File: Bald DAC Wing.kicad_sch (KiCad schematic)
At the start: 29 parts, among them U1 OPA365AIDBVTG4

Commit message: First pass schematic. going to give to clanker to see if it can populate the pcb logically.
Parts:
- added C1, C2, C3, C4: C, Capacitor_SMD:C_0805_2012Metric_Pad1.18x1.45mm_HandSolder, symbol Device:C
- added D1, D2, D3, D4: Power, symbol Device:LED
- added H1, H2, H3, H4: MountingHole_M2.5_Screw, MountingHole:MountingHole_2.7mm_M2.5, symbol My Library:MountingHole_M2.5_Screw
- added J1: Power, symbol Connector_Generic:Conn_01x04
- added J2: DAC_A_Out, symbol Connector_Generic:Conn_01x03
- added J3: DAC_B_Out, symbol Connector_Generic:Conn_01x03
- added R0, R31, R33, R35, R37, R39, R41, R43, R45, R47, R49, R51, R53, R55, R57: 20k, Capacitor_SMD:C_0402_1005Metric_Pad0.74x0.62mm_HandSolder, symbol Device:R
- added R29, R30, R58, R59: 0, Resistor_SMD:R_1206_3216Metric_Pad1.30x1.75mm_HandSolder, symbol Device:R
- added R32, R34, R36, R38, R40, R42, R44, R46, R48, R50, R52, R54, R56: 10k, Capacitor_SMD:C_0402_1005Metric_Pad0.74x0.62mm_HandSolder, symbol Device:R
- added R61, R62, R63, R64: 1k, Resistor_SMD:R_0603_1608Metric_Pad0.98x0.95mm_HandSolder, symbol Device:R
- added TP1, TP2, TP3, TP4, TP5, TP6: TestPoint, My Libraries:Harwin-S1751-46-Test-Point, symbol My Library:TestPoint_Harwin
- added U2: OPA365AIDBVTG4, Package_TO_SOT_SMD:SOT-23-5, symbol Amplifier_Operational:OPA365xxDBV
- R1, R10, R11, R12, R13, R14, R15, R16, R17, R18, R19, R2, R20, R21, R22, R23, R24, R25, R26, R27, R28, R3, R4, R5, R6, R7, R8, R9: footprint (none) -> Capacitor_SMD:C_0402_1005Metric_Pad0.74x0.62mm_HandSolder
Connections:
- net GND: now also C1.2, C2.2, C3.2, C4.2, J1.3 (Pin_3), J1.4 (Pin_4), J2.2 (Pin_2), J2.3 (Pin_3), J3.2 (Pin_2), J3.3 (Pin_3), R31.2, R61.1, R62.1, R63.1, R64.1; no longer U1.2 (V-)
- net VCC: now also C1.1, C2.1, D1.2 (A), D2.2 (A), J1.1 (Pin_1), U2.5 (V+)
- net at R26.2, R27.1: now also R12.2; no longer R13.2
- net at R19.2, R20.1: now also R5.2; no longer R6.2
- net at R20.2, R21.1: now also R6.2; no longer R7.2
- net at R15.1, R28.1: now also R0.2; no longer R1.2
- net at U1.1: now also R29.1; no longer U1.4 (-)
- net at R15.2, R16.1: now also R1.2; no longer R2.2
- net at R21.2, R22.1: now also R7.2; no longer R8.2
- net at R23.2, R24.1: now also R9.2; no longer R10.2
- net at R25.2, R26.1: now also R11.2; no longer R12.2
- net at R22.2, R23.1: now also R8.2; no longer R9.2
- net at R18.2, R19.1: now also R4.2; no longer R5.2
- net at R17.2, R18.1: now also R3.2; no longer R4.2
- net at R24.2, R25.1: now also R10.2; no longer R11.2
- net at R16.2, R17.1: now also R2.2; no longer R3.2
- net D0_LSB renamed A1
- net D1 renamed A2
- net D10 renamed A11
- net D11 renamed A12
- net D12 renamed A13
- net D13_MSB renamed B0
- net D2 renamed A3
- net D3 renamed A4
- net D4 renamed A5
- net D5 renamed A6
- net D6 renamed A7
- net D7 renamed A8
- net D8 renamed A9
- net D9 renamed A10
- removed net VOUT_DAC: R14.2, R27.2, U1.3 (+)
- new net: R40.2, R41.2, R42.1
- new net: R42.2, R43.2, R44.1
- new net: R34.2, R35.2, R36.1
- new net: D4.2 (A), R64.2
- new net: R30.2, TP2.1, U1.3 (+)
- new net: R52.2, R53.2, R54.1
- new net: R44.2, R45.2, R46.1
- new net: R14.2, R31.1, R32.1
- new net: R32.2, R33.2, R34.1
- new net: R50.2, R51.2, R52.1
- new net: R36.2, R37.2, R38.1
- new net: R46.2, R47.2, R48.1
- new net: R58.2, TP5.1, U2.3 (+)
- new net: R54.2, R55.2, R56.1
- new net: R38.2, R39.2, R40.1
- new net: D3.2 (A), R63.2
- new net: R48.2, R49.2, R50.1
- new net: R59.1, U2.1
- new net: D2.1 (K), R62.2
- new net: D1.1 (K), R61.2
- new net A0: R0.1
- new net B1: R33.1
- new net B10: R51.1
- new net B11: R53.1
- new net B12: R55.1
- new net B13: R57.1
- new net B2: R35.1
- new net B3: R37.1
- new net B4: R39.1
- new net B5: R41.1
- new net B6: R43.1
- new net B7: R45.1
- new net B8: R47.1
- new net B9: R49.1
- new net OUT_A: J2.1 (Pin_1), R29.2, TP1.1, U1.4 (-)
- new net OUT_B: J3.1 (Pin_1), R59.2, TP6.1, U2.4 (-)
- new net VEE: C3.1, C4.1, D3.1 (K), D4.1 (K), J1.2 (Pin_2), U1.2 (V-), U2.2 (V-)
- new net VOUT_DAC_A: R13.2, R27.2, R30.1, TP3.1
- new net VOUT_DAC_B: R56.2, R57.2, R58.1, TP4.1
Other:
- note added: "-5"
- note added: "0"
- note added: "Need Blue or White LED to use with 10k. Check price of Green + R cost."
- note added: "Todo: BE Logo Symbol"
- moved on the sheet: R15, R16, R17, R18, R19, R20, R21, R22, R23, R24, R25, R26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

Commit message: bailing on discrete version. makes no sense.
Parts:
- added A1: RaspberryPi_Pico, Module:RaspberryPi_Pico_Common_Unspecified, symbol MCU_Module:RaspberryPi_Pico
- C1, C2, C3, C4: value C -> 1u; LCSC (none) -> C28323
- D1: value Power -> PwrA+; footprint (none) -> LED_SMD:LED_0805_2012Metric_Pad1.15x1.40mm_HandSolder; LCSC (none) -> C7496832
- D2: value Power -> PwrB+; footprint (none) -> LED_SMD:LED_0805_2012Metric_Pad1.15x1.40mm_HandSolder; LCSC (none) -> C7496832
- D3: value Power -> PwrA-; footprint (none) -> LED_SMD:LED_0805_2012Metric_Pad1.15x1.40mm_HandSolder; LCSC (none) -> C7496832
- D4: value Power -> PwrB-; footprint (none) -> LED_SMD:LED_0805_2012Metric_Pad1.15x1.40mm_HandSolder; LCSC (none) -> C7496832
- H1, H2, H3, H4: LCSC (none) -> N/A
- J1: value Power -> Power_In; footprint (none) -> LED_SMD:LED_0805_2012Metric_Pad1.15x1.40mm_HandSolder; LCSC (none) -> N/A
- J2, J3: footprint (none) -> Connector_PinHeader_2.54mm:PinHeader_1x03_P2.54mm_Vertical; LCSC (none) -> N/A
- R61, R62, R63, R64: LCSC C5184071 -> (none)
- TP1, TP2, TP3, TP4, TP5, TP6: LCSC (none) -> C3029083
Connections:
- new net: A1.13 (GND), A1.18 (GND), A1.23 (GND), A1.28 (GND), A1.3 (GND), A1.38 (GND), A1.8 (GND)
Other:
- note added: "1. Need Reset and Boot(how?) buttons on shield. 2. Need 1 signal for blanking. 3. Add Tek probe adapters?"
- note removed: "Need Blue or White LED to use with 10k. Check price of Green + R cost."
- moved on the sheet: H1, H2, H3, H4

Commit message: starting over with ICs
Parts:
- removed R0, R1, R10, R11, R12, R13, R14, R2, R28, R3, R31, R33, R35, R37, R39, R4, R41, R43, R45, R47, R49, R5, R51, R53, R55, R57, R6, R7, R8, R9: 20k, Capacitor_SMD:C_0402_1005Metric_Pad0.74x0.62mm_HandSolder, symbol Device:R
- removed R15, R16, R17, R18, R19, R20, R21, R22, R23, R24, R25, R26, R27, R32, R34, R36, R38, R40, R42, R44, R46, R48, R50, R52, R54, R56: 10k, Capacitor_SMD:C_0402_1005Metric_Pad0.74x0.62mm_HandSolder, symbol Device:R
- removed R29, R30, R58, R59: 0, Resistor_SMD:R_1206_3216Metric_Pad1.30x1.75mm_HandSolder, symbol Device:R
- removed TP1, TP2, TP3, TP4, TP5, TP6: TestPoint, My Libraries:Harwin-S1751-46-Test-Point, symbol My Library:TestPoint_Harwin
- removed U1, U2: OPA365AIDBVTG4, Package_TO_SOT_SMD:SOT-23-5, symbol Amplifier_Operational:OPA365xxDBV
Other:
- note added: "1. Need Reset and Boot(how?) buttons on shield. 2. Need 1 signal for blanking. 3. Add Tek probe adapters? Looking at AD5447 (C514217) 12-bit DAC. Check its datasheet what op-amp buffers it is using."
- note removed: "1. Need Reset and Boot(how?) buttons on shield. 2. Need 1 signal for blanking. 3. Add Tek probe adapters?"

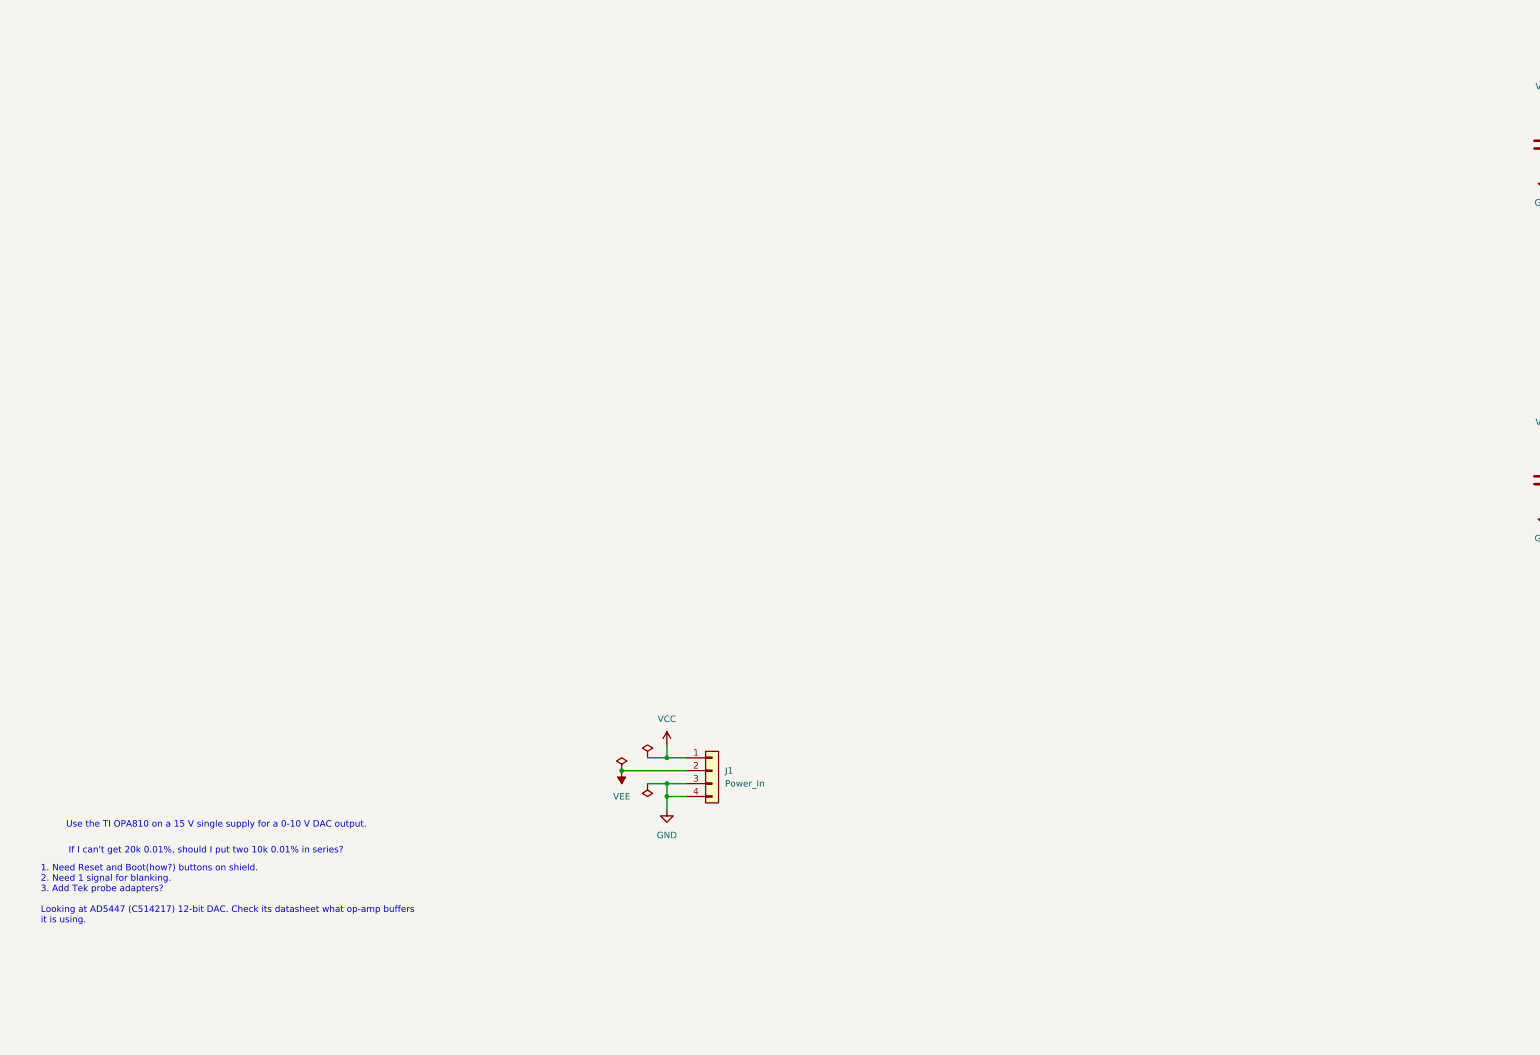
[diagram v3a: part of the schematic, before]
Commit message: latches in place. need to decide on VEE and what to use for Vref (ADR03?)
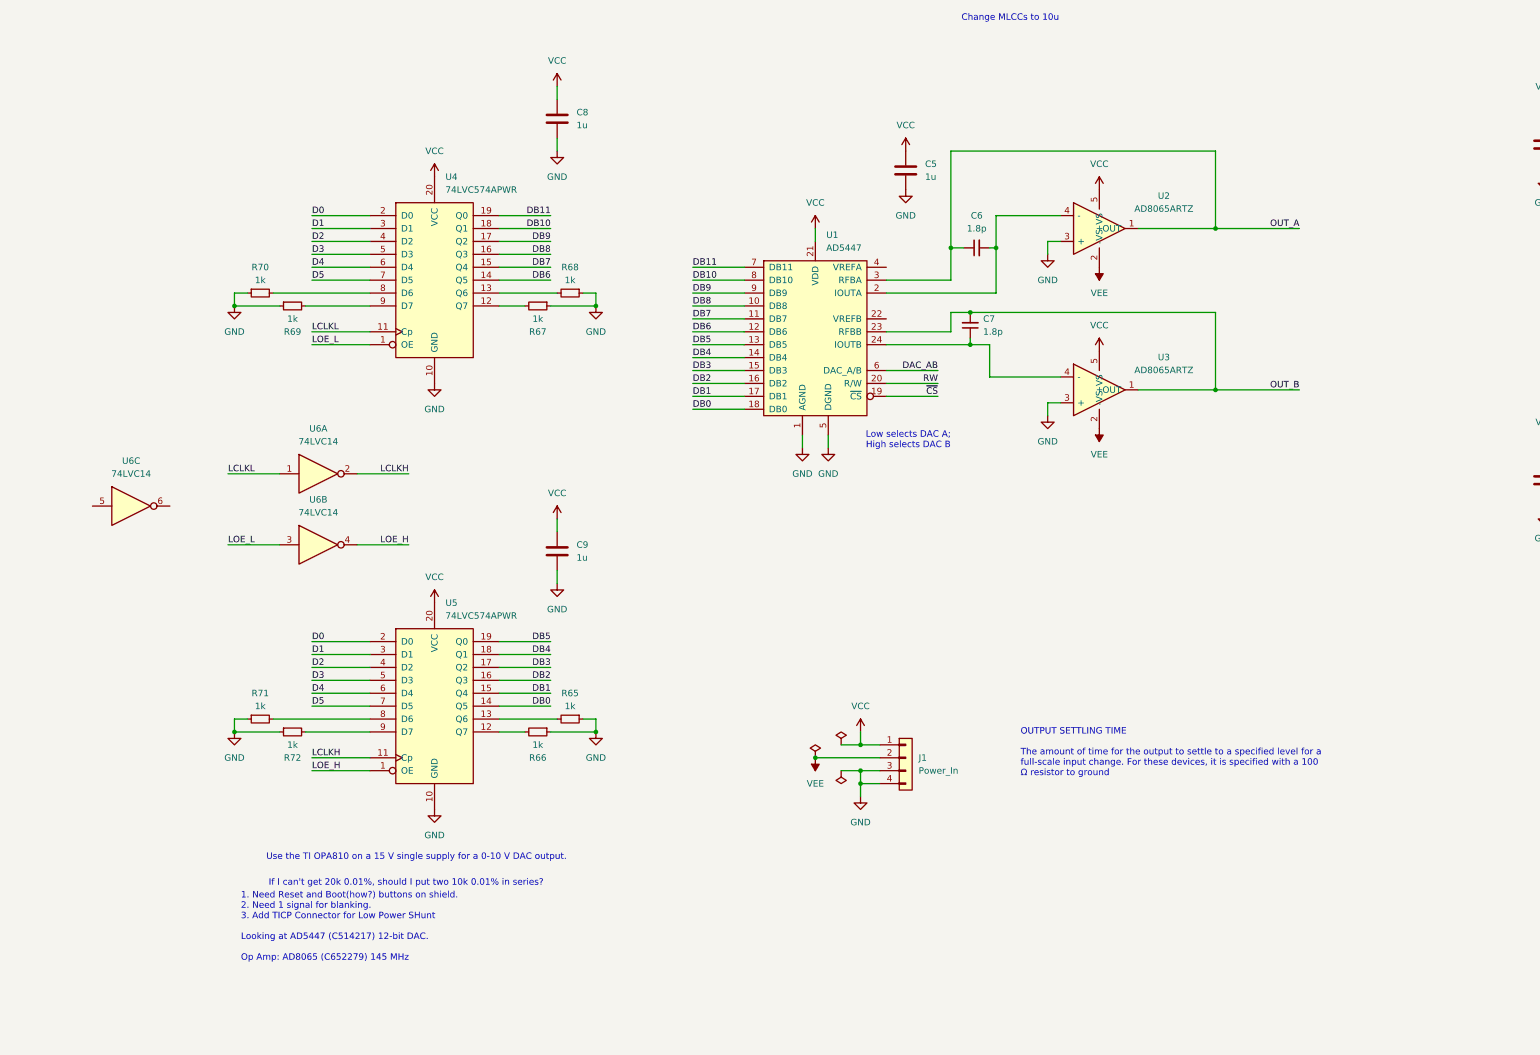
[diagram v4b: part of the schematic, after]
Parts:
- added C5, C8, C9: 1u, Capacitor_SMD:C_0805_2012Metric_Pad1.18x1.45mm_HandSolder, symbol Device:C
- added C6, C7: 1.8p, symbol Device:C_Small
- added R65, R66, R67, R68, R69, R70, R71, R72: 1k, Resistor_SMD:R_0603_1608Metric_Pad0.98x0.95mm_HandSolder, symbol Device:R_Small
- added U1: AD5447, Package_SO:TSSOP-24_4.4x7.8mm_P0.65mm, symbol My Library:AD5447
- added U2, U3: AD8065ARTZ, Package_TO_SOT_SMD:SOT-23-5, symbol My Library:AD8065ARTZ
- added U4, U5: 74LVC574APWR, Package_SO:TSSOP-20_4.4x6.5mm_P0.65mm, symbol 74xx:74HCT574
- added U6: 74LVC14, Package_SO:TSSOP-14_4.4x5mm_P0.65mm, symbol 74xx:74LV14
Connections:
- net GND: now also C5.2, C8.2, C9.2, R65.1, R66.1, R67.1, R68.1, R69.1, R70.1, R71.1, R72.1, U1.1 (AGND), U1.5 (DGND), U2.3 (+), U3.3 (+), U4.10 (GND), U5.10 (GND)
- net OUT_A: now also C6.1, U1.3 (RFBA), U2.1 (OUT)
- net OUT_B: now also C7.2, U1.23 (RFBB), U3.1 (OUT)
- net VCC: now also C5.1, C8.1, C9.1, U1.21 (VDD), U2.5 (+VS), U3.5 (+VS), U4.20 (VCC), U5.20 (VCC)
- net VEE: now also U2.2 (-VS), U3.2 (-VS)
- new net: R67.2, U4.12 (Q7)
- new net: R68.2, U4.13 (Q6)
- new net: R70.2, U4.8 (D6)
- new net: R69.2, U4.9 (D7)
- new net: C6.2, U1.2 (IOUTA), U2.4 (-)
- new net: C7.1, U1.24 (IOUTB), U3.4 (-)
- new net: R72.2, U5.9 (D7)
- new net: R66.2, U5.12 (Q7)
- new net: R65.2, U5.13 (Q6)
- new net: R71.2, U5.8 (D6)
- new net D0: U4.2 (D0), U5.2 (D0)
- new net D1: U4.3 (D1), U5.3 (D1)
- new net D2: U4.4 (D2), U5.4 (D2)
- new net D3: U4.5 (D3), U5.5 (D3)
- new net D4: U4.6 (D4), U5.6 (D4)
- new net D5: U4.7 (D5), U5.7 (D5)
- new net DAC_AB: U1.6 (DAC_A/B)
- new net DB0: U1.18 (DB0), U5.14 (Q5)
- new net DB1: U1.17 (DB1), U5.15 (Q4)
- new net DB10: U1.8 (DB10), U4.18 (Q1)
- new net DB11: U1.7 (DB11), U4.19 (Q0)
- new net DB2: U1.16 (DB2), U5.16 (Q3)
- new net DB3: U1.15 (DB3), U5.17 (Q2)
- new net DB4: U1.14 (DB4), U5.18 (Q1)
- new net DB5: U1.13 (DB5), U5.19 (Q0)
- new net DB6: U1.12 (DB6), U4.14 (Q5)
- new net DB7: U1.11 (DB7), U4.15 (Q4)
- new net DB8: U1.10 (DB8), U4.16 (Q3)
- new net DB9: U1.9 (DB9), U4.17 (Q2)
- new net LCLKH: U5.11 (Cp), U6.2
- new net LCLKL: U4.11 (Cp), U6.1
- new net LOE_H: U5.1 (OE), U6.4
- new net LOE_L: U4.1 (OE), U6.3
- new net RW: U1.20 (R/W)
- new net ~{CS}: U1.19 (~{CS})
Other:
- note added: "1. Need Reset and Boot(how?) buttons on shield. 2. Need 1 signal for blanking. 3. Add TICP Connector for Low Power SHunt Looking at AD5447 (C514217) 12-bit DAC. Op Amp: AD8065 (C652279) 145 MHz"
- note added: "Change MLCCs to 10u"
- note added: "Low selects DAC A; High selects DAC B"
- note added: "OUTPUT SETTLING TIME The amount of time for the output to settle to a specified level for a full-scale input change. For these devices, it is specified with a 100 Ω resistor to ground"
- note removed: "1. Need Reset and Boot(how?) buttons on shield. 2. Need 1 signal for blanking. 3. Add Tek probe adapters? Looking at AD5447 (C514217) 12-bit DAC. Check its datasheet what op-amp buffers it is using."
- moved on the sheet: J1

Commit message: Codex fixes. Check the chat history for examples of good suggestions.
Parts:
- removed R65, R66, R67, R68: 1k, Resistor_SMD:R_0603_1608Metric_Pad0.98x0.95mm_HandSolder, symbol Device:R_Small
- added C10: 1u, Capacitor_SMD:C_0805_2012Metric_Pad1.18x1.45mm_HandSolder, symbol Device:C
- added R73: 1k, Resistor_SMD:R_0603_1608Metric_Pad0.98x0.95mm_HandSolder, symbol Device:R_Small
- added TP1, TP2, TP3, TP4: TestPoint_Harwin, My Libraries:Harwin-S1751-46-Test-Point, symbol My Library:TestPoint_Harwin
- added unit 7 of U6
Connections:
- net GND: now also C10.2, U6.7 (GND)
- net VCC: now also C10.1, R73.2, U6.14 (3.3V)
- net ~{CS}: now also R73.1
- net at U4.12 (Q7): now also TP2.1
- net at U4.13 (Q6): now also TP1.1
- net at U5.12 (Q7): now also TP4.1
- net at U5.13 (Q6): now also TP3.1
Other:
- note added: "TODO: Add V Reference and headers for Vrefs"
- note added: "TODO: Change Pulls to 10k (instead of 1k)"
- note added: "TODO: Pull unused inputs down and add Test points."
- note added: "TODO: Tie RW low. Can't use R because of the latches."
- note added: "TODO: the latches don't need multiplexed OE."

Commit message: added REF3425, low-drop out 2.5v ref
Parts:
- added U7: REF3425, Package_TO_SOT_SMD:SOT-23-6, symbol REF3425:REF3425
- R69, R70, R71, R72, R73: value 1k -> 10k
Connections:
- net RW is gone; now on net GND: U1.20 (R/~{W})
- net LOE_H: no longer names the net of U6.4
- net LOE_H: no longer U5.1 (OE)
- net LOE_L: no longer names the net of U6.3
- net LOE_L: no longer U4.1 (OE)
- new net LOE: U4.1 (OE), U5.1 (OE)
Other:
- note added: "1. Need Reset and Boot(how?) buttons on shield. 2. Need 1 signal for blanking. 3. Add TICP Connector for Low Power SHunt"
- note added: "TODO: Change MLCCs to 10u"
- note removed: "-5"
- note removed: "0"
- note removed: "1. Need Reset and Boot(how?) buttons on shield. 2. Need 1 signal for blanking. 3. Add TICP Connector for Low Power SHunt Looking at AD5447 (C514217) 12-bit DAC. Op Amp: AD8065 (C652279) 145 MHz"
- note removed: "Change MLCCs to 10u"
- note removed: "If I can't get 20k 0.01%, should I put two 10k 0.01% in series?"
- note removed: "Low selects DAC A; High selects DAC B"
- note removed: "TODO: Change Pulls to 10k (instead of 1k)"
- note removed: "TODO: Tie RW low. Can't use R because of the latches."
- note removed: "TODO: the latches don't need multiplexed OE."
- note removed: "Use the TI OPA810 on a 15 V single supply for a 0-10 V DAC output."
- company: (none) -> james@baldengineer.com
- title: (none) -> Bald DAC Wing
- moved on the sheet: A1, C1, C10, C2, C3, C4, C5, C6, C7, C8, C9, D1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
